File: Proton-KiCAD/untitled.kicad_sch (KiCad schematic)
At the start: 24 parts, among them J11 FRONT_BUTTON_1, J12 FRONT_BUTTON_2, J2 KEYPAD, J5 OLED SPI, J6 ROTARY ENCODER, J7 OLED, J8 SI4703

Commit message: finished updated layout
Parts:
- renumbered C32 to C36, C33 to C37, J11 to J10, J5 to J11, J8 to J13, J2 to J5, J6 to J7, J7 to J8, J12 to J9, R16 to R15, R17 to R16, R18 to R17, R19 to R18, R20 to R23, R22 to R24, R23 to R25, R24 to R26, R32 to R36, R31 to R37, R30 to R39
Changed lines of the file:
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@@
 		(on_board yes)
 		(dnp no)
-		(property "Reference" "J12"
+		(property "Reference" "J9"
 			(at 225.425 142.24 0)
 			(effects
@@
 			(project "Proton"
 				(path "/94683f5c-9cd9-448e-be96-9792537b5cb8/3db78fe4-c59d-4a4b-9da7-f2255d3b38e0"
-					(reference "J12")
+					(reference "J9")
 					(unit 1)
 				)
@@
 		(dnp no)
 		(fields_autoplaced yes)
-		(property "Reference" "R24"
+		(property "Reference" "R26"
 			(at 77.47 161.2899 0)
 			(effects
@@
 			(project "Proton"
 				(path "/94683f5c-9cd9-448e-be96-9792537b5cb8/3db78fe4-c59d-4a4b-9da7-f2255d3b38e0"
-					(reference "R24")
+					(reference "R26")
 					(unit 1)
 				)
@@
 		(dnp no)
 		(fields_autoplaced yes)
-		(property "Reference" "R32"
+		(property "Reference" "R36"
 			(at 208.28 110.49 90)
 			(effects
@@
 			(project "Proton"
 				(path "/94683f5c-9cd9-448e-be96-9792537b5cb8/3db78fe4-c59d-4a4b-9da7-f2255d3b38e0"
-					(reference "R32")
+					(reference "R36")
 					(unit 1)
 				)
@@
 		(dnp no)
 		(fields_autoplaced yes)
-		(property "Reference" "R31"
+		(property "Reference" "R37"
 			(at 210.82 140.97 90)
 			(effects
@@
 			(project "Proton"
 				(path "/94683f5c-9cd9-448e-be96-9792537b5cb8/3db78fe4-c59d-4a4b-9da7-f2255d3b38e0"
-					(reference "R31")
+					(reference "R37")
 					(unit 1)
 				)
@@
 		(dnp no)
 		(fields_autoplaced yes)
-		(property "Reference" "C32"
+		(property "Reference" "C36"
 			(at 241.3 59.6899 0)
 			(effects
@@
 			(project "Proton"
 				(path "/94683f5c-9cd9-448e-be96-9792537b5cb8/3db78fe4-c59d-4a4b-9da7-f2255d3b38e0"
-					(reference "C32")
+					(reference "C36")
 					(unit 1)
 				)
@@
 		(dnp no)
 		(fields_autoplaced yes)
-		(property "Reference" "#PWR037"
+		(property "Reference" "#PWR045"
 			(at 63.5 196.85 0)
 			(effects
@@
 			(project "Proton"
 				(path "/94683f5c-9cd9-448e-be96-9792537b5cb8/3db78fe4-c59d-4a4b-9da7-f2255d3b38e0"
-					(reference "#PWR037")
+					(reference "#PWR045")
 					(unit 1)
 				)
@@
 		(on_board yes)
 		(dnp no)
-		(property "Reference" "J6"
+		(property "Reference" "J7"
 			(at 162.052 175.006 0)
 			(effects
@@
 			(project "Proton"
 				(path "/94683f5c-9cd9-448e-be96-9792537b5cb8/3db78fe4-c59d-4a4b-9da7-f2255d3b38e0"
-					(reference "J6")
+					(reference "J7")
 					(unit 1)
 				)
@@
 		(dnp no)
 		(fields_autoplaced yes)
-		(property "Reference" "R30"
+		(property "Reference" "R39"
 			(at 256.54 82.5499 0)
 			(effects
@@
 			(project "Proton"
 				(path "/94683f5c-9cd9-448e-be96-9792537b5cb8/3db78fe4-c59d-4a4b-9da7-f2255d3b38e0"
-					(reference "R30")
+					(reference "R39")
 					(unit 1)
 				)
@@
 		(on_board yes)
 		(dnp no)
-		(property "Reference" "#PWR055"
+		(property "Reference" "#PWR067"
 			(at 261.62 162.56 0)
 			(effects
@@
 			(project "Proton"
 				(path "/94683f5c-9cd9-448e-be96-9792537b5cb8/3db78fe4-c59d-4a4b-9da7-f2255d3b38e0"
-					(reference "#PWR055")
+					(reference "#PWR067")
 					(unit 1)
 				)
@@
 		(dnp no)
 		(fields_autoplaced yes)
-		(property "Reference" "J7"
+		(property "Reference" "J8"
 			(at 225.425 17.78 0)
 			(effects
@@
 			(project "Proton"
 				(path "/94683f5c-9cd9-448e-be96-9792537b5cb8/3db78fe4-c59d-4a4b-9da7-f2255d3b38e0"
-					(reference "J7")
+					(reference "J8")
 					(unit 1)
 				)
@@
 		(dnp no)
 		(fields_autoplaced yes)
-		(property "Reference" "#PWR052"
+		(property "Reference" "#PWR062"
 			(at 232.41 73.66 0)
 			(effects
@@
 			(project "Proton"
 				(path "/94683f5c-9cd9-448e-be96-9792537b5cb8/3db78fe4-c59d-4a4b-9da7-f2255d3b38e0"
-					(reference "#PWR052")
+					(reference "#PWR062")
 					(unit 1)
 				)
@@
 		(dnp no)
 		(fields_autoplaced yes)
-		(property "Reference" "R22"
+		(property "Reference" "R24"
 			(at 69.85 133.35 90)
 			(effects
@@
 			(project "Proton"
 				(path "/94683f5c-9cd9-448e-be96-9792537b5cb8/3db78fe4-c59d-4a4b-9da7-f2255d3b38e0"
-					(reference "R22")
+					(reference "R24")
 					(unit 1)
 				)
@@
 		(dnp no)
 		(fields_autoplaced yes)
-		(property "Reference" "#PWR062"
+		(property "Reference" "#PWR059"
 			(at 212.09 137.16 0)
 			(effects
@@
 			(project "Proton"
 				(path "/94683f5c-9cd9-448e-be96-9792537b5cb8/3db78fe4-c59d-4a4b-9da7-f2255d3b38e0"
-					(reference "#PWR062")
+					(reference "#PWR059")
 					(unit 1)
 				)
@@
 		(dnp no)
 		(fields_autoplaced yes)
-		(property "Reference" "C33"
+		(property "Reference" "C37"
 			(at 252.73 59.6899 0)
 			(effects
@@
 			(project "Proton"
 				(path "/94683f5c-9cd9-448e-be96-9792537b5cb8/3db78fe4-c59d-4a4b-9da7-f2255d3b38e0"
-					(reference "C33")
+					(reference "C37")
 					(unit 1)
 				)
@@
 		(dnp no)
 		(fields_autoplaced yes)
-		(property "Reference" "R23"
+		(property "Reference" "R25"
 			(at 73.66 167.6399 0)
 			(effects
@@
 			(project "Proton"
 				(path "/94683f5c-9cd9-448e-be96-9792537b5cb8/3db78fe4-c59d-4a4b-9da7-f2255d3b38e0"
-					(reference "R23")
+					(reference "R25")
 					(unit 1)
 				)
@@
 		(dnp no)
 		(fields_autoplaced yes)
-		(property "Reference" "R19"
+		(property "Reference" "R18"
 			(at 64.77 135.89 90)
 			(effects
@@
 			(project "Proton"
 				(path "/94683f5c-9cd9-448e-be96-9792537b5cb8/3db78fe4-c59d-4a4b-9da7-f2255d3b38e0"
-					(reference "R19")
+					(reference "R18")
 					(unit 1)
 				)
@@
 		(dnp no)
 		(fields_autoplaced yes)
-		(property "Reference" "R16"
+		(property "Reference" "R15"
 			(at 54.61 140.97 90)
 			(effects
@@
 			(project "Proton"
 				(path "/94683f5c-9cd9-448e-be96-9792537b5cb8/3db78fe4-c59d-4a4b-9da7-f2255d3b38e0"
-					(reference "R16")
+					(reference "R15")
 					(unit 1)
 				)
@@
 		(on_board yes)
 		(dnp no)
-		(property "Reference" "J2"
+		(property "Reference" "J5"
 			(at 22.225 134.62 0)
 			(effects
@@
 			(project "Proton"
 				(path "/94683f5c-9cd9-448e-be96-9792537b5cb8/3db78fe4-c59d-4a4b-9da7-f2255d3b38e0"
-					(reference "J2")
+					(reference "J5")
 					(unit 1)
 				)
@@
 		(dnp no)
 		(fields_autoplaced yes)
-		(property "Reference" "R20"
+		(property "Reference" "R23"
 			(at 69.85 173.9899 0)
 			(effects
@@
 			(project "Proton"
 				(path "/94683f5c-9cd9-448e-be96-9792537b5cb8/3db78fe4-c59d-4a4b-9da7-f2255d3b38e0"
-					(reference "R20")
+					(reference "R23")
 					(unit 1)
 				)
@@
 		(on_board yes)
 		(dnp no)
-		(property "Reference" "#PWR053"
+		(property "Reference" "#PWR064"
 			(at 238.76 153.67 0)
 			(effects
@@
 			(project "Proton"
 				(path "/94683f5c-9cd9-448e-be96-9792537b5cb8/3db78fe4-c59d-4a4b-9da7-f2255d3b38e0"
-					(reference "#PWR053")
+					(reference "#PWR064")
 					(unit 1)
 				)
@@
 		(dnp no)
 		(fields_autoplaced yes)
-		(property "Reference" "#PWR061"
+		(property "Reference" "#PWR060"
 			(at 215.9 165.1 0)
 			(effects
@@
 			(project "Proton"
 				(path "/94683f5c-9cd9-448e-be96-9792537b5cb8/3db78fe4-c59d-4a4b-9da7-f2255d3b38e0"
-					(reference "#PWR061")
+					(reference "#PWR060")
 					(unit 1)
 				)
@@
 		(dnp no)
 		(fields_autoplaced yes)
-		(property "Reference" "R17"
+		(property "Reference" "R16"
 			(at 59.69 138.43 90)
 			(effects
@@
 			(project "Proton"
 				(path "/94683f5c-9cd9-448e-be96-9792537b5cb8/3db78fe4-c59d-4a4b-9da7-f2255d3b38e0"
-					(reference "R17")
+					(reference "R16")
 					(unit 1)
 				)
@@
 		(dnp no)
 		(fields_autoplaced yes)
-		(property "Reference" "R18"
+		(property "Reference" "R17"
 			(at 66.04 180.3399 0)
 			(effects
@@
 			(project "Proton"
 				(path "/94683f5c-9cd9-448e-be96-9792537b5cb8/3db78fe4-c59d-4a4b-9da7-f2255d3b38e0"
-					(reference "R18")
+					(reference "R17")
 					(unit 1)
 				)
@@
 		(on_board yes)
 		(dnp no)
-		(property "Reference" "J11"
+		(property "Reference" "J10"
 			(at 226.695 111.76 0)
 			(effects
@@
 			(project "Proton"
 				(path "/94683f5c-9cd9-448e-be96-9792537b5cb8/3db78fe4-c59d-4a4b-9da7-f2255d3b38e0"
-					(reference "J11")
+					(reference "J10")
 					(unit 1)
 				)
@@
 		(dnp no)
 		(fields_autoplaced yes)
-		(property "Reference" "#PWR050"
+		(property "Reference" "#PWR053"
 			(at 143.51 191.77 0)
 			(effects
@@
 			(project "Proton"
 				(path "/94683f5c-9cd9-448e-be96-9792537b5cb8/3db78fe4-c59d-4a4b-9da7-f2255d3b38e0"
-					(reference "#PWR050")
+					(reference "#PWR053")
 					(unit 1)
 				)
@@
 		(on_board yes)
 		(dnp no)
-		(property "Reference" "#PWR049"
+		(property "Reference" "#PWR051"
 			(at 116.84 172.72 0)
 			(effects
@@
 			(project "Proton"
 				(path "/94683f5c-9cd9-448e-be96-9792537b5cb8/3db78fe4-c59d-4a4b-9da7-f2255d3b38e0"
-					(reference "#PWR049")
+					(reference "#PWR051")
 					(unit 1)
 				)
@@
 		(on_board yes)
 		(dnp no)
-		(property "Reference" "J8"
+		(property "Reference" "J13"
 			(at 271.145 129.54 0)
 			(effects
@@
 			(project "Proton"
 				(path "/94683f5c-9cd9-448e-be96-9792537b5cb8/3db78fe4-c59d-4a4b-9da7-f2255d3b38e0"
-					(reference "J8")
+					(reference "J13")
 					(unit 1)
 				)
@@
 		(on_board yes)
 		(dnp no)
-		(property "Reference" "J5"
+		(property "Reference" "J11"
 			(at 227.33 87.376 0)
 			(effects
@@
 			(project "Proton"
 				(path "/94683f5c-9cd9-448e-be96-9792537b5cb8/3db78fe4-c59d-4a4b-9da7-f2255d3b38e0"
-					(reference "J5")
+					(reference "J11")
 					(unit 1)
 				)
@@
 		(on_board yes)
 		(dnp no)
-		(property "Reference" "#PWR054"
+		(property "Reference" "#PWR065"
 			(at 248.92 36.83 0)
 			(effects
@@
 			(project "Proton"
 				(path "/94683f5c-9cd9-448e-be96-9792537b5cb8/3db78fe4-c59d-4a4b-9da7-f2255d3b38e0"
-					(reference "#PWR054")
+					(reference "#PWR065")
 					(unit 1)
 				)
@@
 		(on_board yes)
 		(dnp no)
-		(property "Reference" "#PWR051"
+		(property "Reference" "#PWR066"
 			(at 254 81.28 0)
 			(effects
@@
 			(project "Proton"
 				(path "/94683f5c-9cd9-448e-be96-9792537b5cb8/3db78fe4-c59d-4a4b-9da7-f2255d3b38e0"
-					(reference "#PWR051")
-					(unit 1)
-				)
+					(reference "#PWR066")
+					(unit 1)
+				)

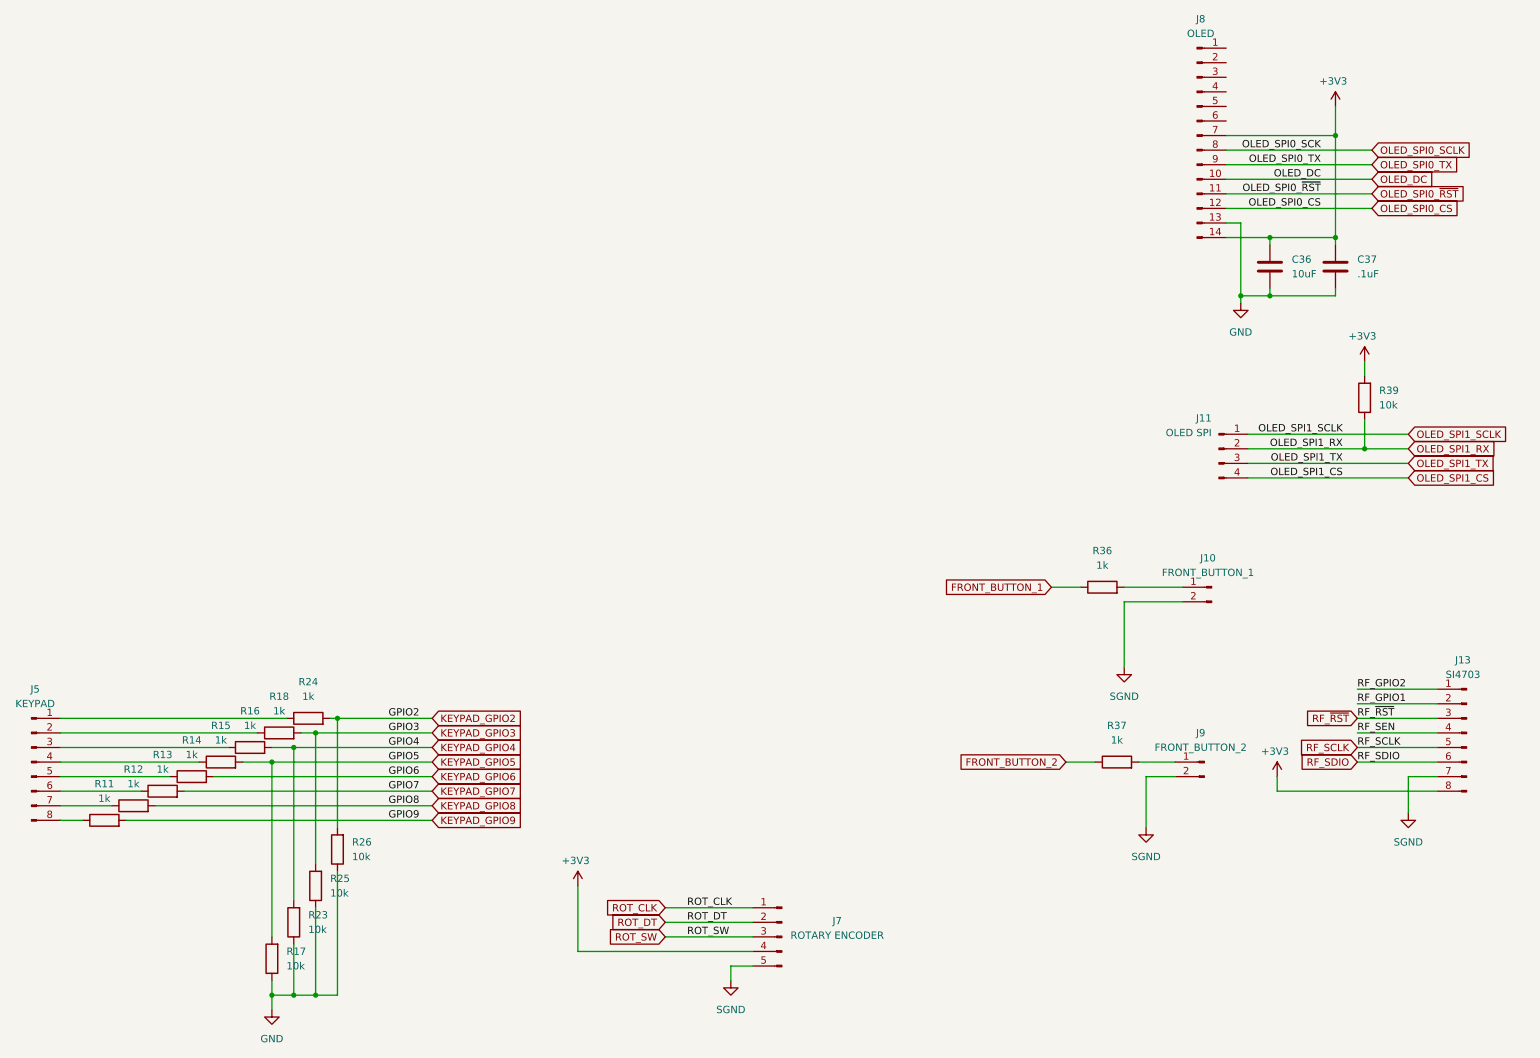
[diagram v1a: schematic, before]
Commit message: BOM and CPL changes
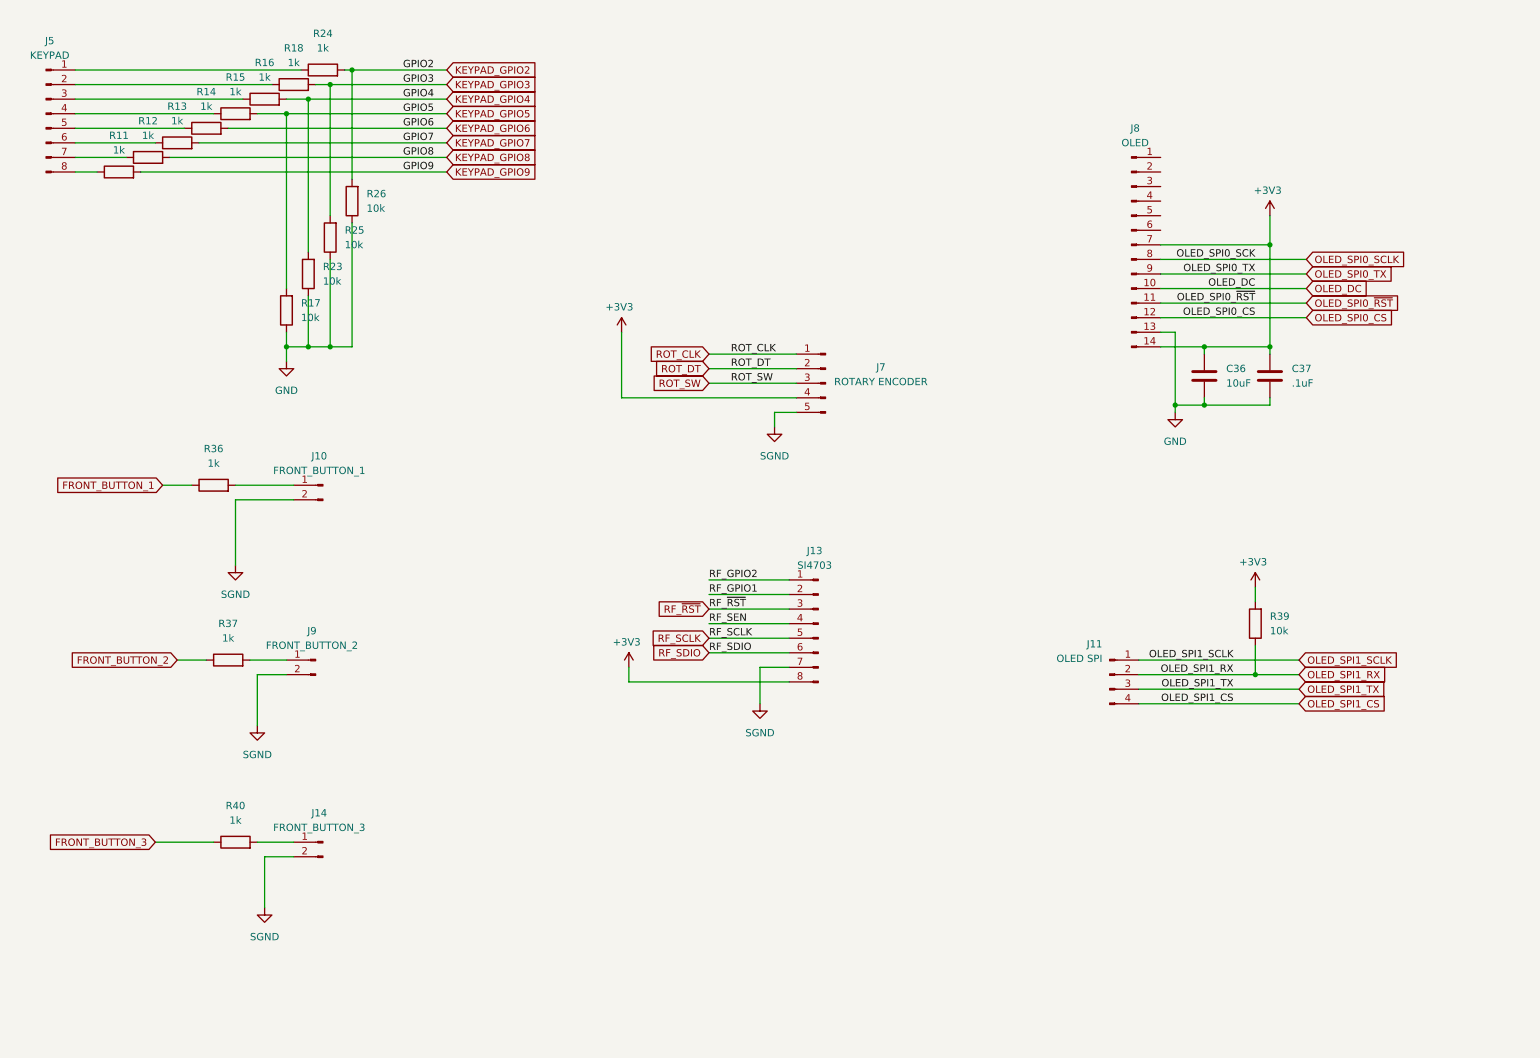
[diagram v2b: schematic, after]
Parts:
- added J14: FRONT_BUTTON_3, Connector_PinHeader_2.54mm:PinHeader_1x02_P2.54mm_Vertical, symbol Connector:Conn_01x02_Pin
- added R40: 1k, Resistor_SMD:R_0402_1005Metric, symbol Device:R
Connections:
- net SGND: now also J14.2 (Pin_2)
- new net: J14.1 (Pin_1), R40.2
- new net FRONT_BUTTON_3: R40.1
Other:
- moved on the sheet: C36, C37, J10, J11, J13, J5, J7, J8, J9, R11, R12, R13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

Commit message: changing for basic pedal
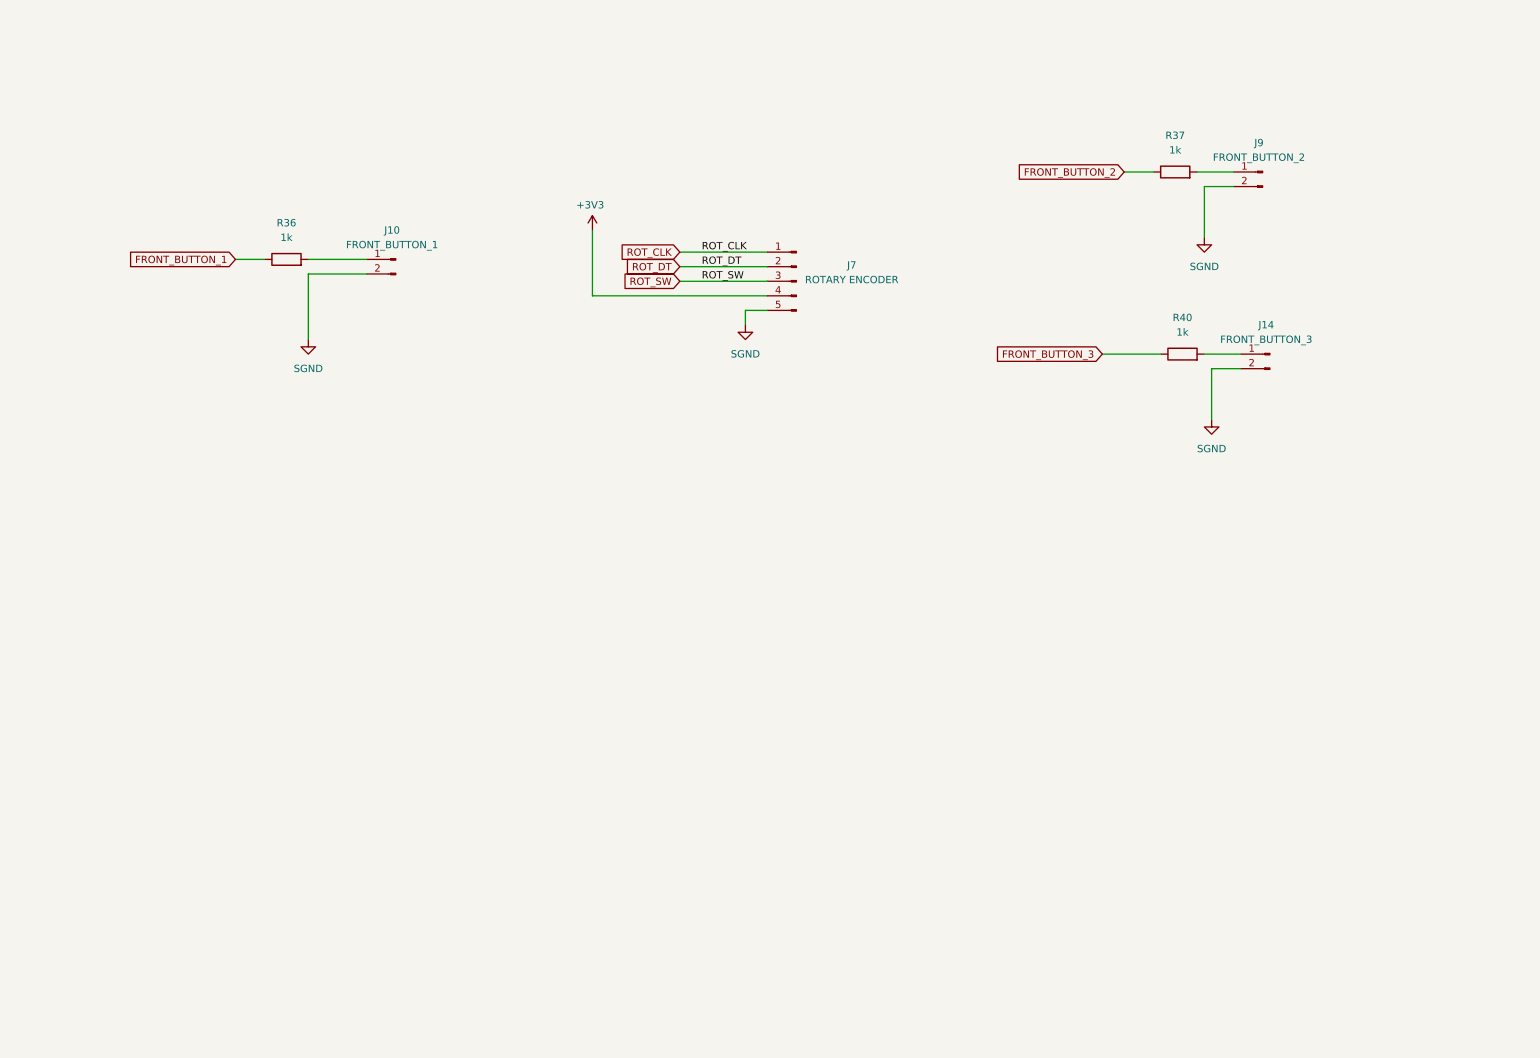
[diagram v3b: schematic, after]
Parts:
- removed C36: 10uF, Capacitor_SMD:C_0805_2012Metric, symbol Device:C
- removed C37: .1uF, Capacitor_SMD:C_0402_1005Metric, symbol Device:C
- removed J11: OLED SPI, Connector_PinHeader_2.54mm:PinHeader_1x04_P2.54mm_Vertical, symbol Connector:Conn_01x04_Pin
- removed J13: SI4703, Connector_PinHeader_2.54mm:PinHeader_1x08_P2.54mm_Vertical, symbol Connector:Conn_01x08_Pin
- removed J5: KEYPAD, Connector_PinHeader_2.54mm:PinHeader_1x08_P2.54mm_Vertical, symbol Connector:Conn_01x08_Pin
- removed J8: OLED, Connector_PinHeader_2.54mm:PinHeader_1x14_P2.54mm_Vertical, symbol Connector:Conn_01x14_Pin
- removed R11, R12, R13, R14, R15, R16, R18, R24: 1k, Resistor_SMD:R_0402_1005Metric, symbol Device:R
- removed R17, R23, R25, R26, R39: 10k, Resistor_SMD:R_0402_1005Metric, symbol Device:R
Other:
- moved on the sheet: J10, J14, J7, J9, R36, R37, R40
